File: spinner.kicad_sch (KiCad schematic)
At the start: 114 parts, among them J1 Micro_SD_Card, SW1 SW_SPDT, U1 AP63205WU, U2 RS0102, U3 SFH617A-3X006, U4 SFH617A-3X006, U5 SFH617A-3X006, U6 ESP32-WROVER, u10 ESP32-S3-WROOM-1

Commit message: Hooked up the BMS and wrote some notes.  Gonna be fire!
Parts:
- added D? (x2): LED, symbol Device:LED
- added R? (x2): 1.5k, symbol Device:R
- added R?: 590, symbol Device:R
- added R?: 1.1k, symbol Device:R
- added R?: 10k, symbol Device:R
- added U?: BQ24073RGT, Package_DFN_QFN:VQFN-16-1EP_3x3mm_P0.5mm_EP1.6x1.6mm, symbol Battery_Management:BQ24073RGT
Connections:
- net +3V3: now also U?.5 (EN2)
- net +BATT: now also BT2.1 (+), BT3.1 (+), U?.2 (BAT), U?.3 (BAT)
- net GND: now also BT1.2 (-), BT2.2 (-), R?.2, R?.2, R?.2, U?.14 (TMR), U?.15 (TD), U?.17 (VSS), U?.4 (~{CE}), U?.6 (EN1), U?.8 (VSS)
- new net: R?.1, R?.1, U?.10 (OUT), U?.11 (OUT)
- new net: D?.2 (A), R?.2 (x2)
- new net: R?.1, U?.1 (TS)
- new net: R?.1, U?.12 (ILIM)
- new net: R?.1, U?.16 (ISET)
- new net CHG_L: D?.1 (K), U?.9 (~{CHG})
- new net PGOOD_L: D?.1 (K), U?.7 (~{PGOOD})
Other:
- moved on the sheet: BT2, BT3

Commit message: Moving all the version 9.0
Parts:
- I1, I2: value IDC -> 1; Spice_Model dc(1) -> (none); Spice_Netlist_Enabled Y -> (none); Spice_Primitive I -> (none)

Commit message: Layout things.
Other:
- moved on the sheet: BT2, BT3
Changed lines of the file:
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@@
 	)
 	(junction
+		(at 49.53 27.94)
+		(diameter 0)
+		(color 0 0 0 0)
+	)
+	(junction
 		(at 80.01 39.37)
 		(diameter 0)
@@
 	)
 	(junction
+		(at 17.78 27.94)
+		(diameter 0)
+		(color 0 0 0 0)
+	)
+	(junction
 		(at 190.5 261.62)
 		(diameter 0)
@@
 	)
 	(junction
+		(at 31.75 20.32)
+		(diameter 0)
+		(color 0 0 0 0)
+	)
+	(junction
 		(at 148.59 248.92)
 		(diameter 0)
@@
 	)
 	(junction
+		(at 49.53 20.32)
+		(diameter 0)
+		(color 0 0 0 0)
+	)
+	(junction
 		(at 58.42 176.53)
 		(diameter 0)
@@
 	)
 	(junction
+		(at 17.78 20.32)
+		(diameter 0)
+		(color 0 0 0 0)
+	)
+	(junction
 		(at 43.18 205.74)
 		(diameter 0)
@@
 	)
 	(junction
+		(at 31.75 27.94)
+		(diameter 0)
+		(color 0 0 0 0)
+	)
+	(junction
 		(at 55.88 130.81)
 		(diameter 0)
@@
 	(wire
 		(pts
+			(xy 17.78 20.32) (xy 31.75 20.32)
+		)
+		(stroke
+			(width 0)
+			(type default)
+		)
+	)
+	(wire
+		(pts
 			(xy 43.18 246.38) (xy 76.2 246.38)
 		)
@@
 	(wire
 		(pts
+			(xy 31.75 27.94) (xy 49.53 27.94)
+		)
+		(stroke
+			(width 0)
+			(type default)
+		)
+	)
+	(wire
+		(pts
 			(xy 53.34 135.89) (xy 54.61 135.89)
 		)
@@
 	(wire
 		(pts
+			(xy 17.78 27.94) (xy 31.75 27.94)
+		)
+		(stroke
+			(width 0)
+			(type default)
+		)
+	)
+	(wire
+		(pts
 			(xy 53.34 160.02) (xy 54.61 160.02)
 		)
@@
 	(wire
 		(pts
+			(xy 31.75 20.32) (xy 49.53 20.32)
+		)
+		(stroke
+			(width 0)
+			(type default)
+		)
+	)
+	(wire
+		(pts
 			(xy 154.94 100.33) (xy 160.02 100.33)
 		)
@@
 	(symbol
 		(lib_id "power:GND")
-		(at 30.48 46.99 0)
+		(at 49.53 27.94 0)
 		(unit 1)
 		(exclude_from_sim no)
@@
 		(fields_autoplaced yes)
 		(property "Reference" "#PWR045"
-			(at 30.48 53.34 0)
+			(at 49.53 34.29 0)
 			(effects
 				(font
@@
 		)
 		(property "Value" "GND"
-			(at 30.48 52.07 0)
+			(at 49.53 33.02 0)
 			(effects
 				(font
@@
 		)
 		(property "Footprint" ""
-			(at 30.48 46.99 0)
+			(at 49.53 27.94 0)
 			(effects
 				(font
@@
 		)
 		(property "Datasheet" ""
-			(at 30.48 46.99 0)
+			(at 49.53 27.94 0)
 			(effects
 				(font
@@
 		)
 		(property "Description" ""
-			(at 30.48 46.99 0)
+			(at 49.53 27.94 0)
 			(effects
 				(font
@@
 	(symbol
 		(lib_id "power:+BATT")
-		(at 44.45 20.32 0)
+		(at 31.75 20.32 0)
 		(unit 1)
 		(exclude_from_sim no)
@@
 		(fields_autoplaced yes)
 		(property "Reference" "#PWR?"
-			(at 44.45 24.13 0)
+			(at 31.75 24.13 0)
 			(effects
 				(font
@@
 		)
 		(property "Value" "+BATT"
-			(at 44.45 15.24 0)
+			(at 31.75 15.24 0)
 			(effects
 				(font
@@
 		)
 		(property "Footprint" ""
-			(at 44.45 20.32 0)
+			(at 31.75 20.32 0)
 			(effects
 				(font
@@
 		)
 		(property "Datasheet" ""
-			(at 44.45 20.32 0)
+			(at 31.75 20.32 0)
 			(effects
 				(font
@@
 		)
 		(property "Description" ""
-			(at 44.45 20.32 0)
+			(at 31.75 20.32 0)
 			(effects
 				(font
@@
 	(symbol
 		(lib_id "Device:Battery_Cell")
-		(at 44.45 25.4 0)
+		(at 31.75 25.4 0)
 		(unit 1)
 		(exclude_from_sim no)
@@
 		(fields_autoplaced yes)
 		(property "Reference" "BT2"
-			(at 48.26 22.0979 0)
+			(at 35.56 22.0979 0)
 			(effects
 				(font
@@
 		)
 		(property "Value" "Battery_Cell"
-			(at 48.26 24.6379 0)
+			(at 35.56 24.6379 0)
 			(effects
 				(font
@@
 		)
 		(property "Footprint" "Library:Spinner_BatteryHolder_Keystone_2460_1xAA"
-			(at 44.45 23.876 90)
+			(at 31.75 23.876 90)
 			(effects
 				(font
@@
 		)
 		(property "Datasheet" "~"
-			(at 44.45 23.876 90)
+			(at 31.75 23.876 90)
 			(effects
 				(font
@@
 		)
 		(property "Description" ""
-			(at 44.45 25.4 0)
+			(at 31.75 25.4 0)
 			(effects
 				(font
@@
 	(symbol
 		(lib_id "power:GND")
-		(at 44.45 27.94 0)
+		(at 31.75 27.94 0)
 		(unit 1)
 		(exclude_from_sim no)
@@
 		(fields_autoplaced yes)
 		(property "Reference" "#PWR?"
-			(at 44.45 34.29 0)
+			(at 31.75 34.29 0)
 			(effects
 				(font
@@
 		)
 		(property "Value" "GND"
-			(at 44.45 33.02 0)
+			(at 31.75 33.02 0)
 			(effects
 				(font
@@
 		)
 		(property "Footprint" ""
-			(at 44.45 27.94 0)
+			(at 31.75 27.94 0)
 			(effects
 				(font
@@
 		)
 		(property "Datasheet" ""
-			(at 44.45 27.94 0)
+			(at 31.75 27.94 0)
 			(effects
 				(font
@@
 		)
 		(property "Description" ""
-			(at 44.45 27.94 0)
+			(at 31.75 27.94 0)
 			(effects
 				(font
@@
 	(symbol
 		(lib_id "Device:Battery_Cell")
-		(at 30.48 44.45 0)
+		(at 49.53 25.4 0)
 		(unit 1)
 		(exclude_from_sim no)
@@
 		(fields_autoplaced yes)
 		(property "Reference" "BT3"
-			(at 34.29 41.1479 0)
+			(at 53.34 22.0979 0)
 			(effects
 				(font
@@
 		)
 		(property "Value" "Battery_Cell"
-			(at 34.29 43.6879 0)
+			(at 53.34 24.6379 0)
 			(effects
 				(font
@@
 		)
 		(property "Footprint" "Library:Spinner_BatteryHolder_Keystone_2460_1xAA"
-			(at 30.48 42.926 90)
+			(at 49.53 23.876 90)
 			(effects
 				(font
@@
 		)
 		(property "Datasheet" "~"
-			(at 30.48 42.926 90)
+			(at 49.53 23.876 90)
 			(effects
 				(font
@@
 		)
 		(property "Description" ""
-			(at 30.48 44.45 0)
+			(at 49.53 25.4 0)
 			(effects
 				(font
@@
 	(symbol
 		(lib_id "power:+BATT")
-		(at 30.48 39.37 0)
+		(at 49.53 20.32 0)
 		(unit 1)
 		(exclude_from_sim no)
@@
 		(fields_autoplaced yes)
 		(property "Reference" "#PWR?"
-			(at 30.48 43.18 0)
+			(at 49.53 24.13 0)
 			(effects
 				(font
@@
 		)
 		(property "Value" "+BATT"
-			(at 30.48 34.29 0)
+			(at 49.53 15.24 0)
 			(effects
 				(font
@@
 		)
 		(property "Footprint" ""
-			(at 30.48 39.37 0)
+			(at 49.53 20.32 0)
 			(effects
 				(font
@@
 		)
 		(property "Datasheet" ""
-			(at 30.48 39.37 0)
+			(at 49.53 20.32 0)
 			(effects
 				(font
@@
 		)
 		(property "Description" ""
-			(at 30.48 39.37 0)
+			(at 49.53 20.32 0)
 			(effects
 				(font

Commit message: IDK.  Add LDO n stuff.
Issue:  HAKZ-100
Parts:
- removed H4, H5, H6, H7, H8, H9: MountingHole, MountingHole:MountingHole_3mm, symbol Mechanical:MountingHole
- removed U6: ESP32-WROVER, Library:ESP32-WROVER, symbol hakz:ESP32-WROVER
- added J301: USB_C_Receptacle_USB2.0_16P, Connector_USB:USB_C_Receptacle_GCT_USB4105-xx-A_16P_TopMnt_Horizontal, symbol Connector:USB_C_Receptacle_USB2.0_16P
- added R306, R307: 5.1k, Resistor_SMD:R_0603_1608Metric, symbol Device:R
- added U302: SPX3819M5-L-3-3, Package_TO_SOT_SMD:SOT-23-5, symbol Regulator_Linear:SPX3819M5-L-3-3
- u10: footprint Library:ESP32-S3-WROOM-1U -> Library:ESP32-S3-WROOM-1
- gave numbers to parts that had none: 8
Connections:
- net +3V3: now also U302.5 (OUT)
- net GND: now also J301.A1 (GND), J301.A12 (GND), J301.B1 (GND), J301.B12 (GND), J301.S1 (SHIELD), R306.2, R307.2, U302.2 (GND)
- net usb_d-: now reaches u10.13 (GPIO19/U1RTS/ADC2_CH8/CLK_OUT2/USB_D-)
- net usb_d-: now also J301.A7 (D-), J301.B7 (D-)
- net usb_d+: now reaches u10.14 (GPIO20/U1CTS/ADC2_CH9/CLK_OUT1/USB_D+)
- net usb_d+: now also J301.A6 (D+), J301.B6 (D+)
- new net: U302.1 (IN), U302.3 (EN)
- new net: J301.B5 (CC2), R307.1
- new net: J301.A5 (CC1), R306.1
- new net: J301.A4 (VBUS), J301.A9 (VBUS), J301.B4 (VBUS), J301.B9 (VBUS)

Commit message: Add more parts and things.  Power stage is done!!  Tots works.
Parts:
- removed C1, C2: 22uF, Capacitor_SMD:C_0805_2012Metric_Pad1.18x1.45mm_HandSolder, symbol Device:C_Polarized
- removed C3: .1uF, Capacitor_SMD:C_0805_2012Metric_Pad1.18x1.45mm_HandSolder, symbol Device:C
- removed L1: 4.7uH, Inductor_SMD:L_0805_2012Metric_Pad1.05x1.20mm_HandSolder, symbol Device:L
- removed U1: AP63205WU, Package_TO_SOT_SMD:TSOT-23-6, symbol Regulator_Switching:AP63205WU
- added C5: 10uF, Capacitor_SMD:C_0805_2012Metric_Pad1.18x1.45mm_HandSolder, symbol Device:C_Polarized
- added C6, C7: 22uF, Capacitor_SMD:C_0805_2012Metric_Pad1.18x1.45mm_HandSolder, symbol Device:C_Polarized
- added C8: 10nF, Capacitor_SMD:C_0805_2012Metric, symbol Device:C_Polarized
- added F301: Polyfuse_Small, symbol Device:Polyfuse_Small
- added J302: Conn_01x02_Pin, symbol Connector:Conn_01x02_Pin
- added JP301: SolderJumper_3_Bridged12, Jumper:SolderJumper-3_P1.3mm_Bridged12_RoundedPad1.0x1.5mm, symbol Jumper:SolderJumper_3_Bridged12
- added L2: 1 uH, Inductor_SMD:L_Coilcraft_XAL7030-102, symbol Device:L
- added R308: 732k, Resistor_SMD:R_0805_2012Metric, symbol Device:R
- added R309: 100k, Resistor_SMD:R_0805_2012Metric, symbol Device:R
- added U303: TPS61022, Package_DFN_QFN:Texas_RWU0007A_VQFN-7_2x2mm_P0.5mm, symbol Converter_DCDC:TPS61022
- C4: value 10uF -> 22uF
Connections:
- net +3V3: no longer U301.5 (EN2)
- net +BATT: now also U301.5 (EN2), F301.1; no longer BT1.1 (+), BT2.1 (+), BT3.1 (+), SW1.2 (B)
- net GND: now also SW1.1 (A), C5.2, C6.2, C7.2, C8.2, JP301.1 (A), R309.2, U303.1 (GND)
- net BATT_COND: now reaches R305.1, U301.10 (OUT), U301.11 (OUT)
- net BATT_COND: now also SW1.3 (C), C5.1, JP301.3 (B), L2.1, U303.7 (VIN); no longer R304.1
- net +5V: now reaches U302.1 (IN), U302.3 (EN)
- net +5V: now also C4.1, R304.1, C6.1, C7.1, R308.1, U303.3 (VOUT)
- net at U302.4 (BP): now also C8.1
- new net: R308.2, R309.1, U303.4 (FB)
- new net: JP301.2 (C), U303.6 (MODE)
- new net: F301.2, J302.1 (Pin_1)
- new net: BT1.1 (+), BT2.1 (+), BT3.1 (+), J302.2 (Pin_2)
- new net: L2.2, U303.2 (SW)
- new net: SW1.2 (B), U303.5 (EN)
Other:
- note added: "B00ST +5v"
- note added: "BMS"
- note added: "LDO - 3.3"
- moved on the sheet: BT1, BT2, BT3, C4, D325, D326, R301, R302, R303, R304, R305, SW1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

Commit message: Decided to ditch the bounce beam.  Added labels to SD and USB.
Amazing resitor layout.  Ditched resitor network.
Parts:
- removed RN1: R_Network08, Resistor_SMD:R_Array_Convex_5x1206, symbol Device:R_Network08
- removed U5: SFH617A-3X006, Library:tcrt1000, symbol Isolator:SFH617A-3X006
- added R4, R5, R6, R7, R8, R9: 10k, Resistor_SMD:R_0805_2012Metric_Pad1.20x1.40mm_HandSolder, symbol Device:R
- added U6: SFH617A-3X006, Library:MULTI_PART_THRU_BEAM, symbol Isolator:SFH617A-3X006
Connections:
- net +3V3: now also R4.1, R5.1, R6.1, R7.1, R8.1, R9.1
- net GND: now also U6.2, U6.4
- net OPTO_in_2: now also U6.3
- net spi_clk: now also R7.2
- net V USB: now reaches U301.13 (IN)
- net V USB: now also J301.A4 (VBUS), J301.A9 (VBUS), J301.B4 (VBUS), J301.B9 (VBUS)
- net at U3.2: now also U6.1
- net dat_1: now reaches J1.8 (DAT1)
- net dat_1: now also R9.2
- net dat_2: now reaches J1.1 (DAT2)
- net dat_2: now also R4.2
- net GPIO_13: no longer names the net of U2.7 (A1)
- net GPIO_14: no longer names the net of U2.6 (A2)
- net spi_cs renamed dat_3
- net dat_3: now also R5.2
- net spi_in renamed dat_0
- net dat_0: now also R8.2
- net spi_out renamed cmd
- net cmd: now also R6.2
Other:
- note added: "B00ST 5v"
- note added: "LDO 3.3"
- note added: "SD"
- note added: "USB-C"
- note removed: "B00ST +5v"
- note removed: "LDO - 3.3"
- moved on the sheet: J1, J301, R306, R307, TP1, TP2, TP3, TP4, TP5, TP6, TP7, TP8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

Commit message: Did the things... and happiness.
Placed through beam, boost circuit layout, labeled done things.
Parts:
- added I3: 1, Diode_SMD:D_SOD-123, symbol Simulation_SPICE:IDC
- renumbered U3 to TB1, U4 to TB2, U6 to TB3
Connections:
- net DI: now also D0.6 (DO), D101.1 (DI)
- net GND: now also TB1.2
- net VCC: now also I3.1
- net at TB3.1: now also I3.2; no longer TB1.2
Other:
- note added: "Level Shifter"
- note added: "Mount Points"
- note added: "Spoke 1"
- note added: "Spoke 2"
- note added: "Spoke 3"
- note added: "Through Beams"
- moved on the sheet: D0, D101, D102, D103, D104, D105, D106, D107, D108, D109, D110, D111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

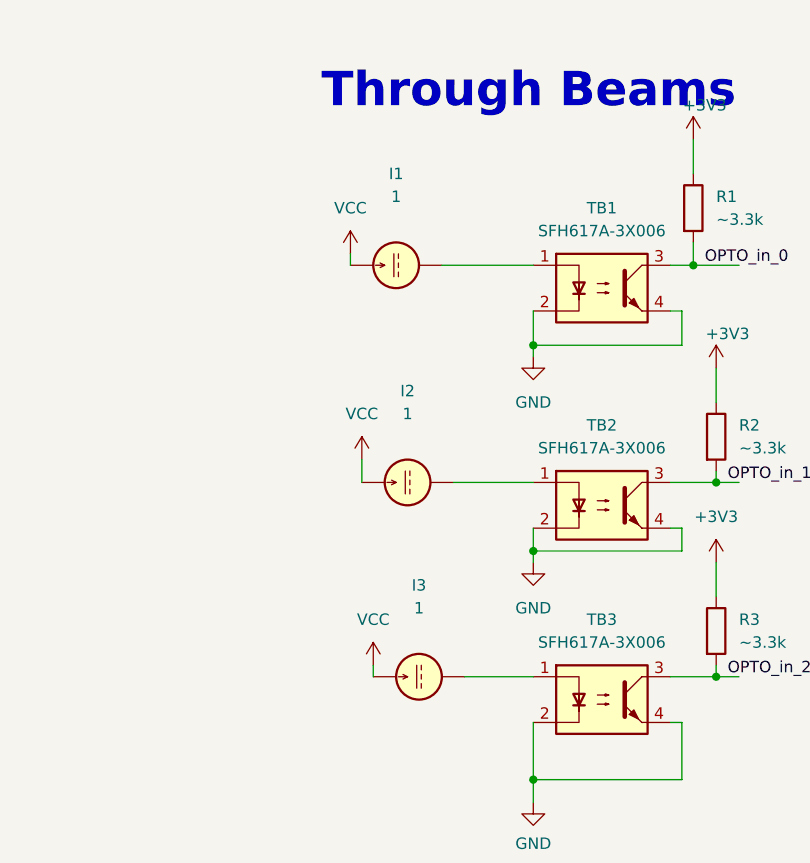
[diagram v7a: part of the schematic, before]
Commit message: Add a datasheet and make a few connections.  etc.
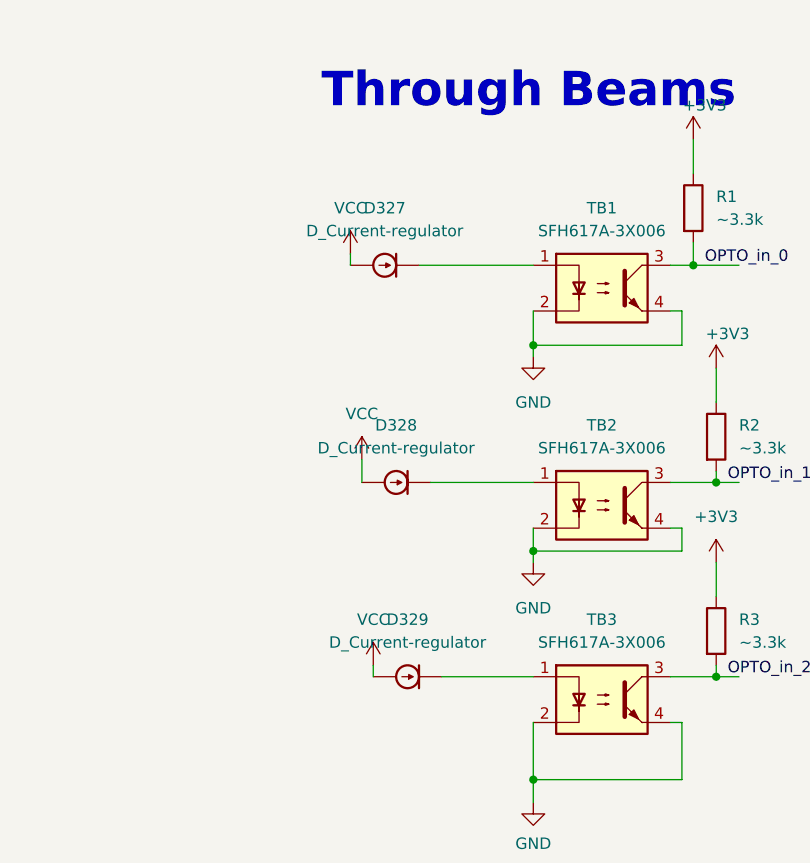
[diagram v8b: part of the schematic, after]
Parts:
- removed I1, I2, I3: 1, Diode_SMD:D_SOD-123, symbol Simulation_SPICE:IDC
- added D327, D328, D329: D_Current-regulator, Diode_SMD:D_SOD-123, symbol Device:D_Current-regulator
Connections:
- net VCC: now also D327.2 (A), D328.2 (A), D329.2 (A)
- net at TB3.1: now also D329.1 (K)
- net at TB1.1: now also D327.1 (K)
- net at TB2.1: now also D328.1 (K)
